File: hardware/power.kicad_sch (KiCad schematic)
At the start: 25 parts, among them J3 Battery, U9 MCP73811T-420I-OT

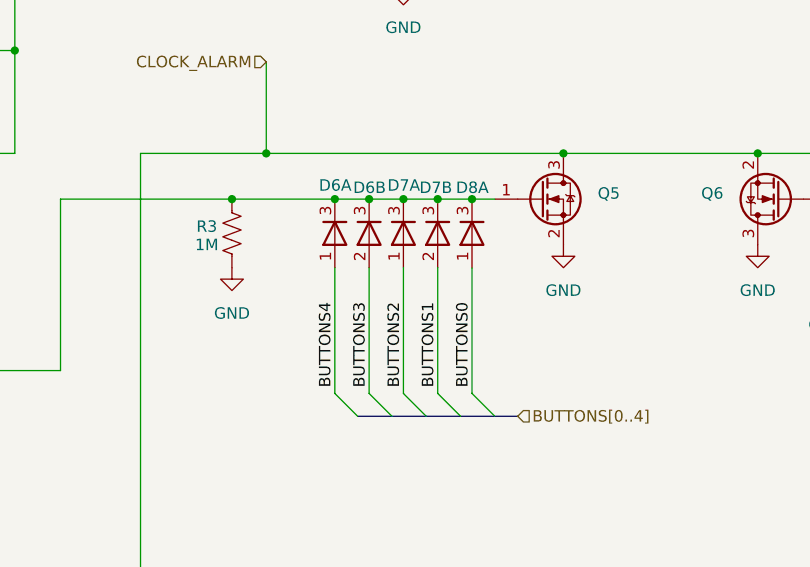
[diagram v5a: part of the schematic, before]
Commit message: Resized cartridge and moved around things
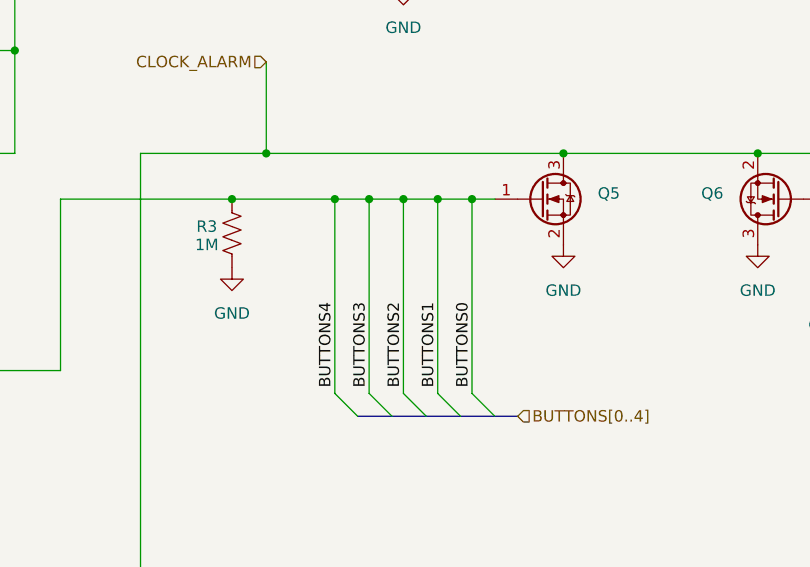
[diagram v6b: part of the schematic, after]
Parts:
- removed D6, D7: D_Dual_CommonCathode_AAK_Split, Package_TO_SOT_SMD:SOT-23, symbol Device:D_Dual_CommonCathode_AAK_Split
- removed unit 1 of D8
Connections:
- net BUTTONS0: now also Q2.3 (D), Q5.1 (G), R3.1

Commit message: Almost done TM
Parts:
- removed D8: D_Dual_CommonCathode_AAK_Split, Package_TO_SOT_SMD:SOT-23, symbol Device:D_Dual_CommonCathode_AAK_Split
- removed J3: Battery, boombox:EBAA02C, symbol Connector_Generic:Conn_01x02
- added TP6, TP7: TestPoint_Small, boombox:TestPoint_Pad_2.0x2.0mm, symbol Connector:TestPoint_Small
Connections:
- net GND: now also TP7.1
- net at D12.2 (A), U9.3 (V_{BAT}): now also TP6.1
- net BUTTONS0 renamed BTN_LATCH
- no-connect marks 4 -> 2
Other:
- note added: "Battery"

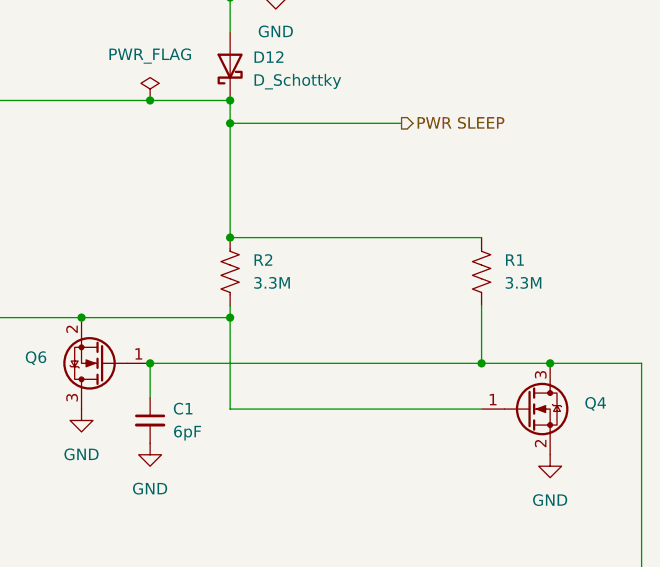
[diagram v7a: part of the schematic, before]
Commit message: Reading from SD card
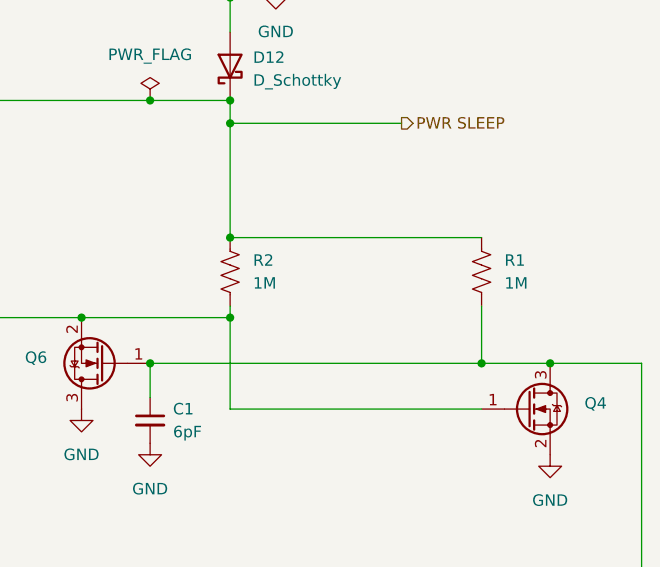
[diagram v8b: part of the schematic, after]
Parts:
- R1, R2: value 3.3M -> 1M
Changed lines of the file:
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@@
 			)
 		)
-		(property "Value" "3.3M"
+		(property "Value" "1M"
 			(at 210.82 66.0399 0)
 			(effects
@@
 			)
 		)
-		(property "Value" "3.3M"
+		(property "Value" "1M"
 			(at 238.76 66.0399 0)
 			(effects
